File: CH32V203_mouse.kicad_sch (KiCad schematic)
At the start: 0 parts

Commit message: MCU placed decoupling capacitors labels added
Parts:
- added C1: 4u7, symbol Device:C
- added C2, C3: 100n, symbol Device:C
- added U1: CH32V203G6U6, Package_DFN_QFN:QFN-28-1EP_4x4mm_P0.4mm_EP2.8x2.8mm, symbol CH32V203:CH32V203G6U6
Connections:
- new net: C1.1, C2.1, C3.1
- new net: C1.2, C2.2, C3.2, U1.17 (VDD), U1.5 (VDDA)
- new net BOOT0: U1.1 (BOOT0/PB8)
- new net GND: U1.16 (VSS), U1.29 (VSS)
- new net NRST: U1.4 (NRST)
- new net OSC_IN: U1.2 (OSC_IN/PD0)
- new net OSC_OUT: U1.3 (OSC_OUT/PD1)
- new net SWCLK: U1.22 (PA14/SWCLK)
- new net SWDIO: U1.21 (PA13/SWDIO)
- new net USB_DM: U1.19 (PA10/PA11/USB1DM)
- new net USB_DP: U1.20 (PA12/USB1DP)
- no-connect marks 0 -> 17
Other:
- note added: "MCU"

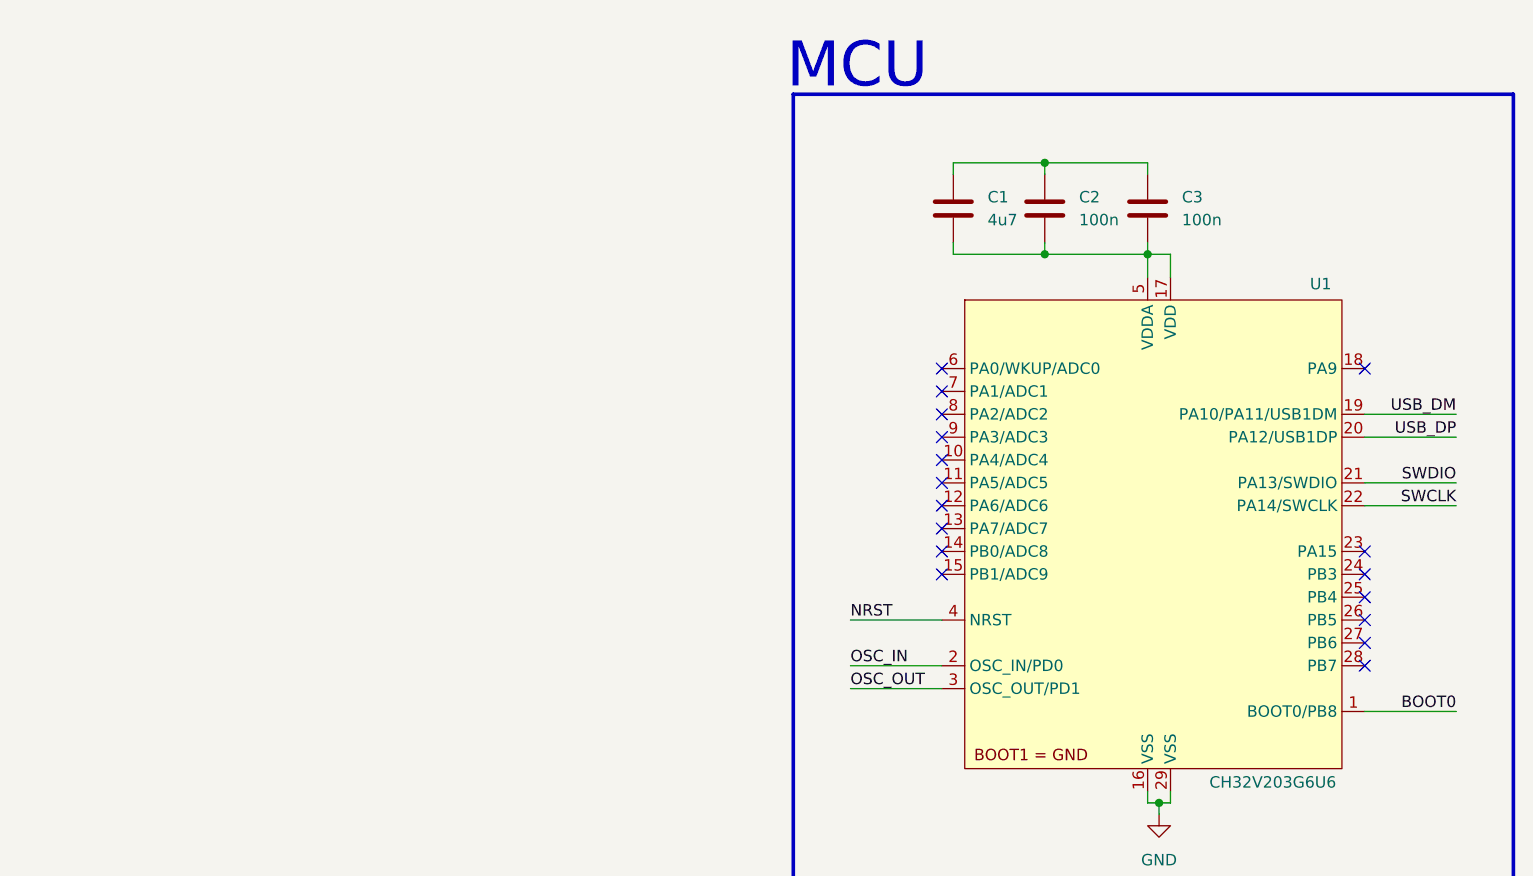
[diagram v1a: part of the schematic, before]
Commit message: 3V3 supply using an LDO
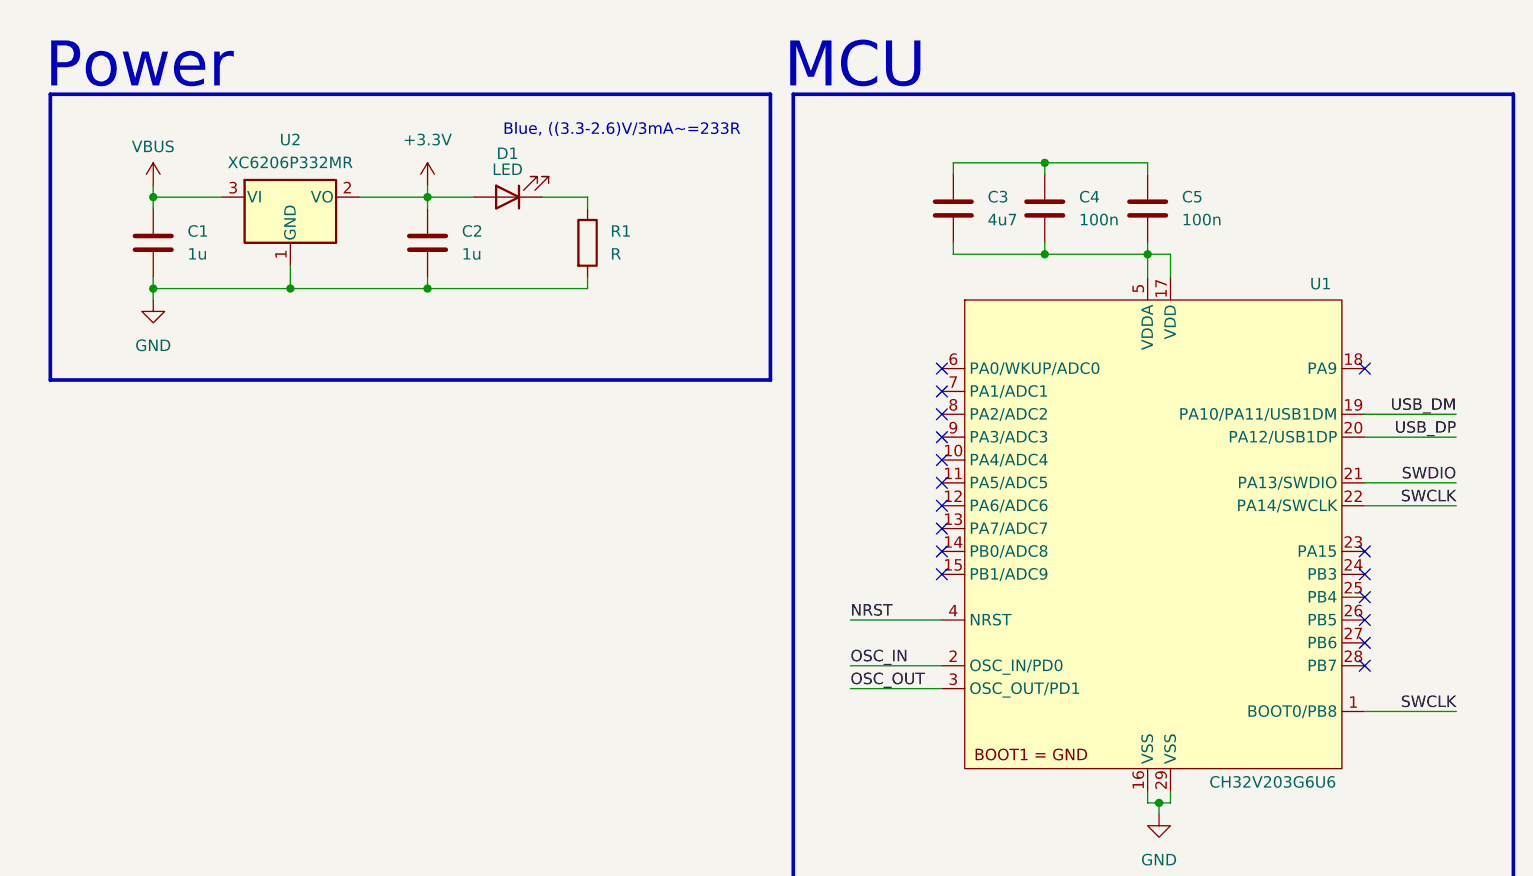
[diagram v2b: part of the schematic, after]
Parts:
- added C1, C2: 1u, symbol Device:C
- added D1: LED, symbol Device:LED
- added R1: R, symbol Device:R
- added U2: XC6206P332MR, Package_TO_SOT_SMD:SOT-23-3, symbol Regulator_Linear:XC6206PxxxMR
- renumbered C1 to C3, C2 to C4, C3 to C5
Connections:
- net BOOT0 is gone; now on net SWCLK: U1.1 (BOOT0/PB8)
- net GND: now also C1.2, C2.2, R1.2, U2.1 (GND)
- new net: D1.1 (K), R1.1
- new net +3.3V: C2.1, D1.2 (A), U2.2 (VO)
- new net VBUS: C1.1, U2.3 (VI)
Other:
- note added: "Blue, ((3.3-2.6)V/3mA~=233R"
- note added: "Power"

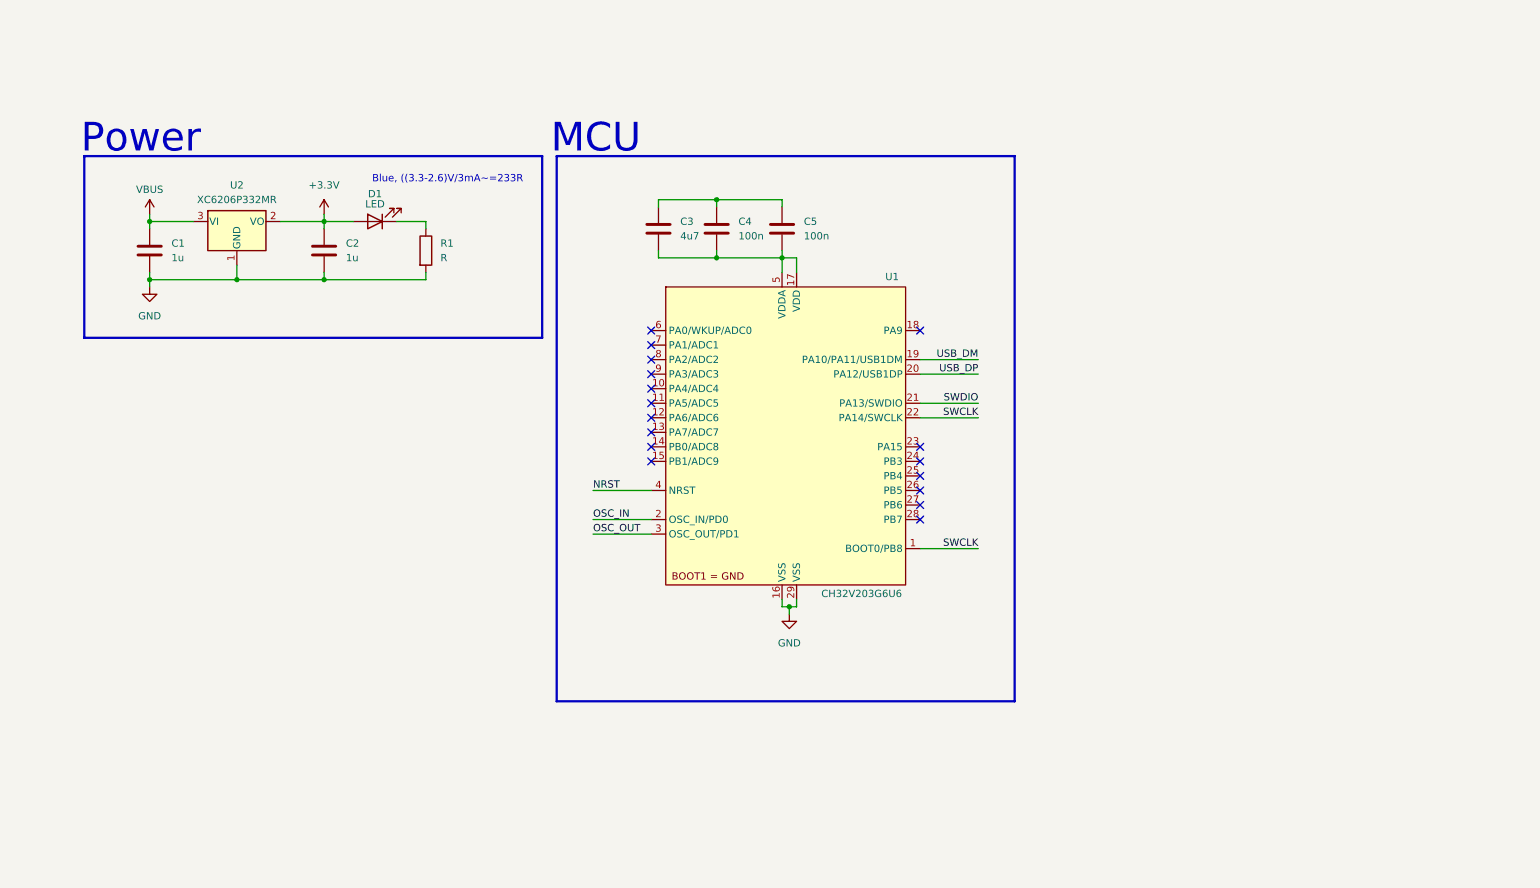
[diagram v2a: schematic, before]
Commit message: USB type C receptacle, ESD protection ON LED current changed to 2mA, 330R resistor selected net labels
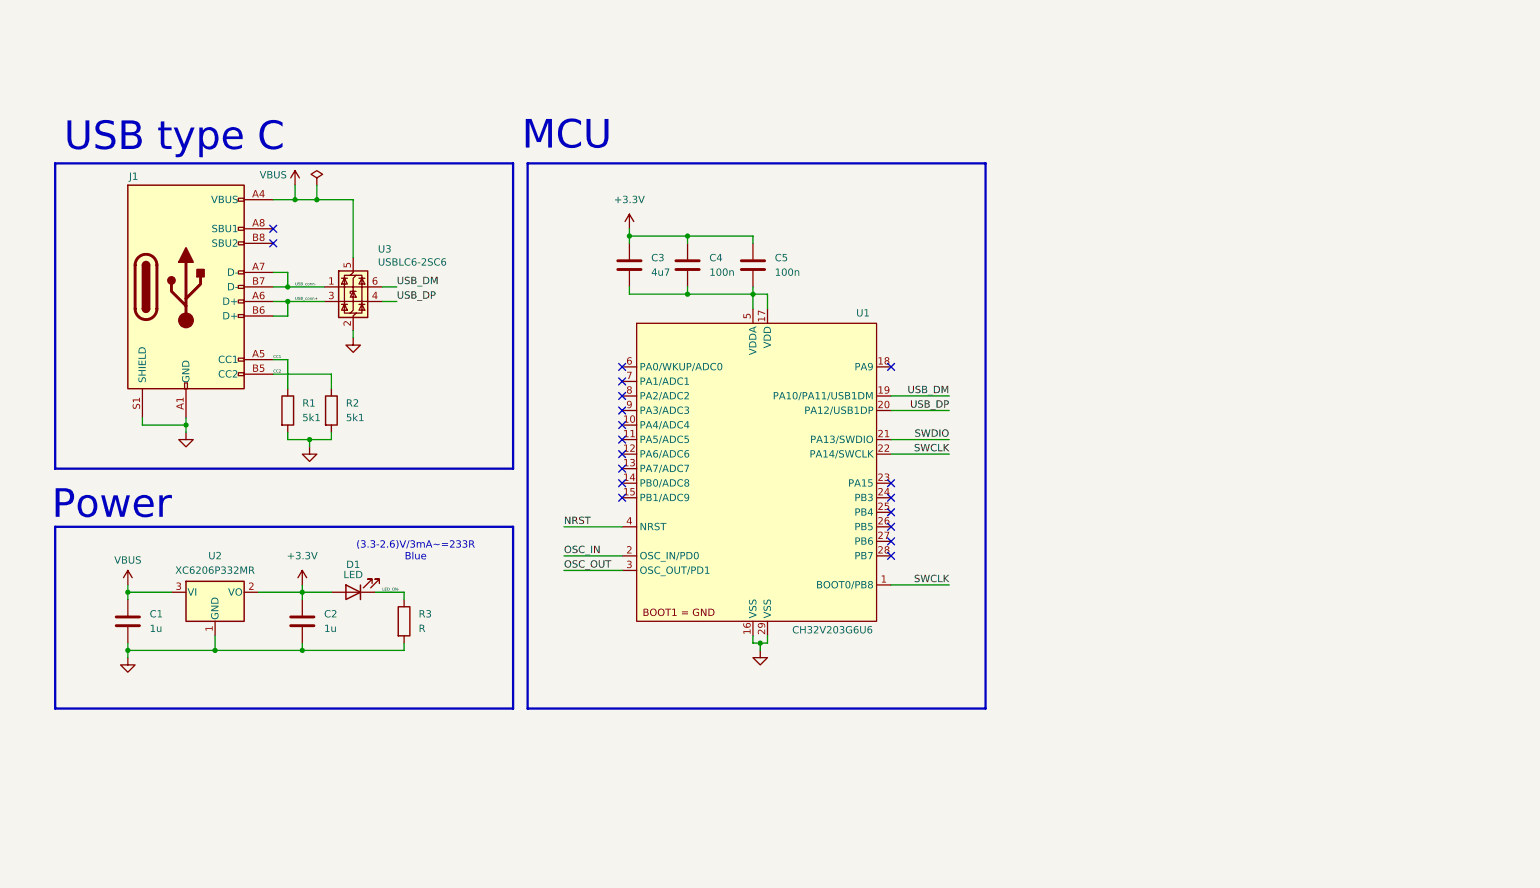
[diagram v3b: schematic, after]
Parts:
- added J1: USB_C_Receptacle_USB2.0_16P_updated, symbol USB_C:USB_C_Receptacle_USB2.0_16P_updated
- added R1, R2: 5k1, symbol Device:R
- added U3: USBLC6-2SC6, Package_TO_SOT_SMD:SOT-23-6, symbol Power_Protection:USBLC6-2SC6
- renumbered R1 to R3
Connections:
- net +3.3V: now also C3.1, C4.1, C5.1
- net GND: now also J1.A1 (GND), J1.A12 (GND), J1.B1 (GND), J1.B12 (GND), J1.S1 (SHIELD), R1.2, R2.2, U3.2 (GND)
- net USB_DM: now also U3.6 (I/O1)
- net USB_DP: now also U3.4 (I/O2)
- net VBUS: now also J1.A4 (VBUS), J1.A9 (VBUS), J1.B4 (VBUS), J1.B9 (VBUS), U3.5 (VBUS)
- net LED_ON-: now reaches D1.1 (K), R3.1
- new net CC1: J1.A5 (CC1), R1.1
- new net CC2: J1.B5 (CC2), R2.1
- new net USB_conn+: J1.A6 (D+), J1.B6 (D+), U3.3 (I/O2)
- new net USB_conn-: J1.A7 (D-), J1.B7 (D-), U3.1 (I/O1)
- no-connect marks 17 -> 19
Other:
- note added: "(3.3-2.6)V/3mA~=233R Blue"
- note added: "USB type C"
- note removed: "Blue, ((3.3-2.6)V/3mA~=233R"
- moved on the sheet: C1, C2, C3, C4, C5, D1, R3, U1, U2

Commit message: Crystal oscillator circuit
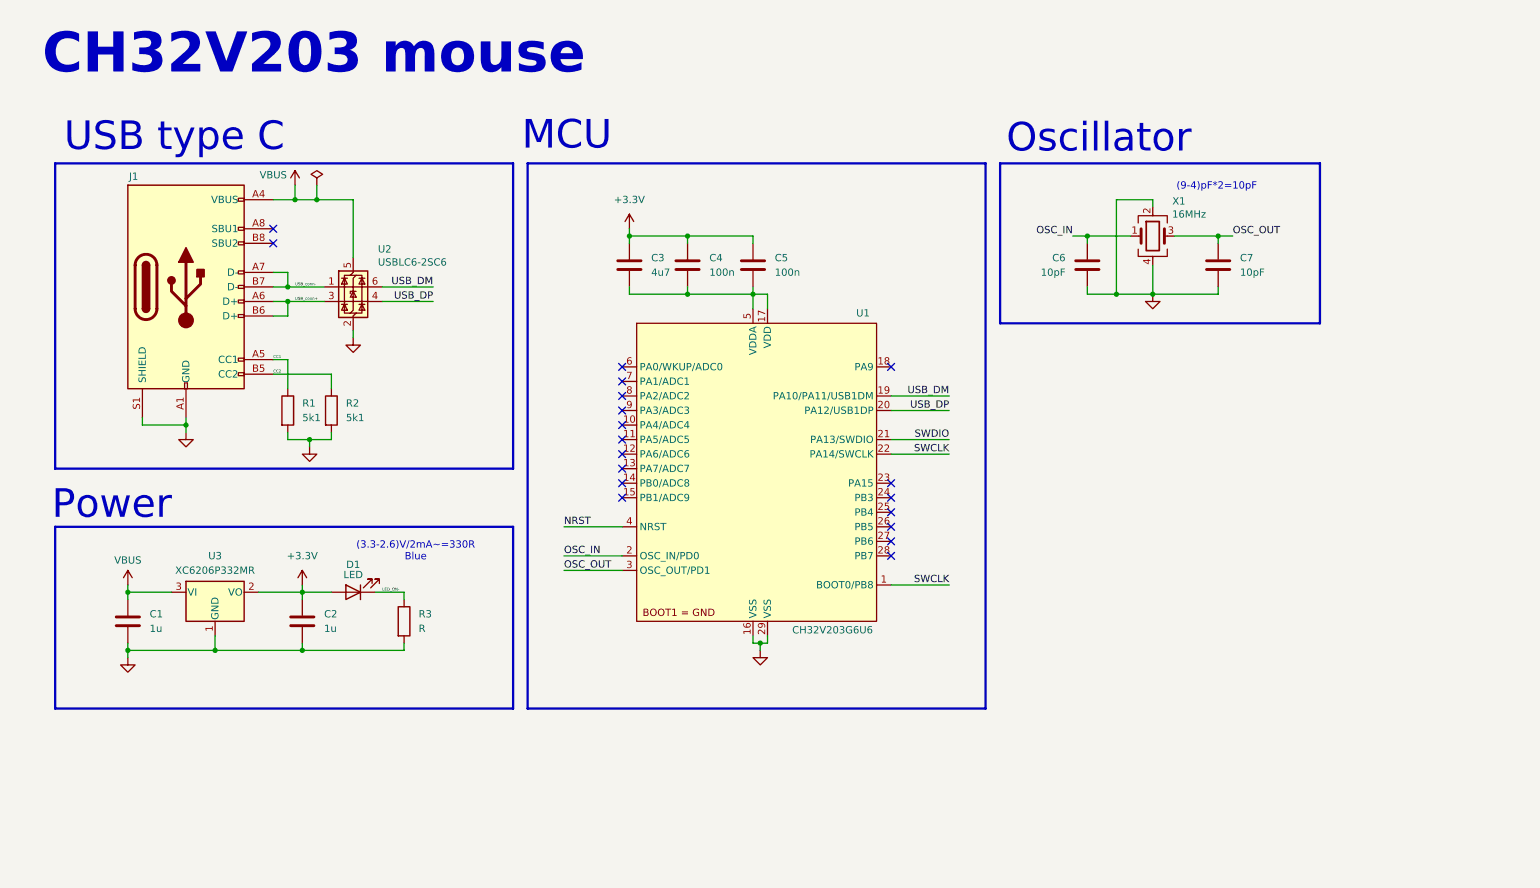
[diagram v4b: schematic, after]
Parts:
- added C6, C7: 10pF, symbol Device:C
- added X1: 16MHz, symbol Device:Crystal_GND24
- renumbered U3 to U2, U2 to U3
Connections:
- net GND: now also C6.2, C7.2, X1.2, X1.4
- net OSC_IN: now also C6.1, X1.1
- net OSC_OUT: now also C7.1, X1.3
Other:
- note added: "(3.3-2.6)V/2mA~=330R Blue"
- note added: "(9-4)pF*2=10pF"
- note added: "CH32V203 mouse"
- note added: "Oscillator"
- note removed: "(3.3-2.6)V/3mA~=233R Blue"

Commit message: Status LED placed changed color of power on LED to red
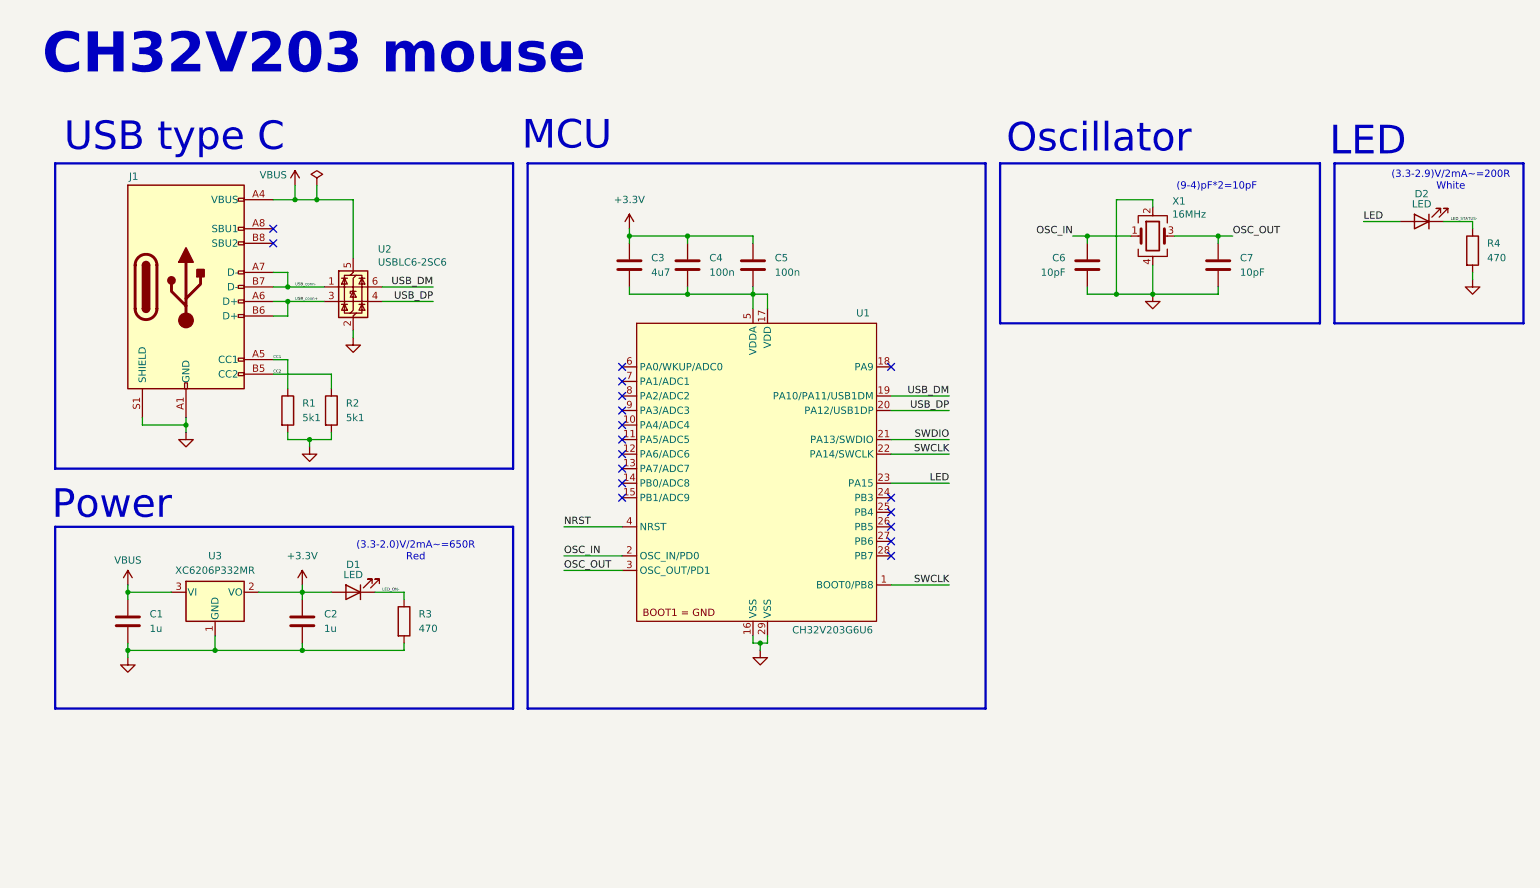
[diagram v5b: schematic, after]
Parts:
- added D2: LED, symbol Device:LED
- added R4: 470, symbol Device:R
- R3: value R -> 470
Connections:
- net GND: now also R4.2
- net LED: now reaches U1.23 (PA15)
- net LED: now also D2.2 (A)
- new net LED_STATUS-: D2.1 (K), R4.1
- no-connect marks 19 -> 18
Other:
- note added: "(3.3-2.0)V/2mA~=650R Red"
- note added: "(3.3-2.9)V/2mA~=200R White"
- note added: "LED"
- note removed: "(3.3-2.6)V/2mA~=330R Blue"
